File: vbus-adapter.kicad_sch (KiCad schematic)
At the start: 50 parts, among them J1 VBUS, J2 CAN, J3 Sens 2, J4 Sens 1, J5 Power, J6 Backup GPIO, J7 Program, Q1 SS8050, Q2 SS8050, T800 AO3400A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

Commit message: Fix footprint for C802
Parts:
- C802: footprint Capacitor_SMD:CP_Elec_4x3.9 -> Capacitor_SMD:CP_Elec_8x10
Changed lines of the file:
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@@
 			)
 		)
-		(property "Footprint" "Capacitor_SMD:CP_Elec_4x3.9"
+		(property "Footprint" "Capacitor_SMD:CP_Elec_8x10"
 			(at 157.1752 43.18 0)
 			(effects
@@
 			(at 156.21 39.37 0)
 			(effects
+				(font
+					(size 1.27 1.27)
+				)
+				(hide yes)
+			)
+		)
+		(property "Untitled Field" ""
+			(at 156.21 39.37 0)
+			(effects

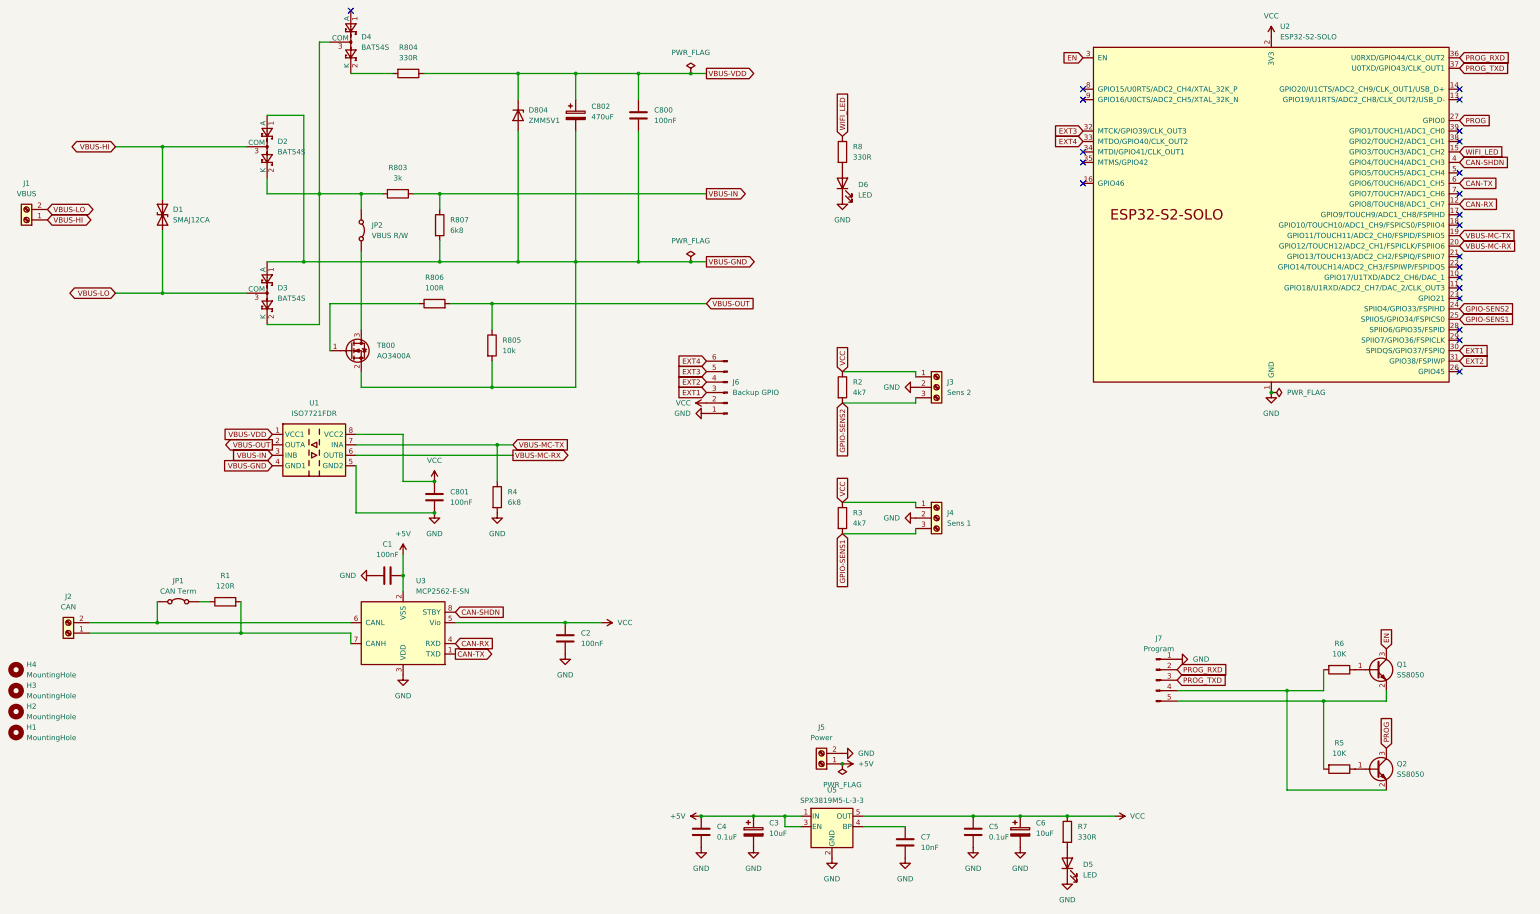
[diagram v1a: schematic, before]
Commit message: Fixed power connection for U3 (MCP2562) Changed Z-Diode to BZY55B5V1RBG with 0805 pinout Added 10k pullup to ESP32 EN pin Added 1uF capacitor to ESP32 EN pin Added 100nF and 10uF capacitor to ESP32 Vcc pin Replaced 0.1uF capacitor values to 100nF for consistency
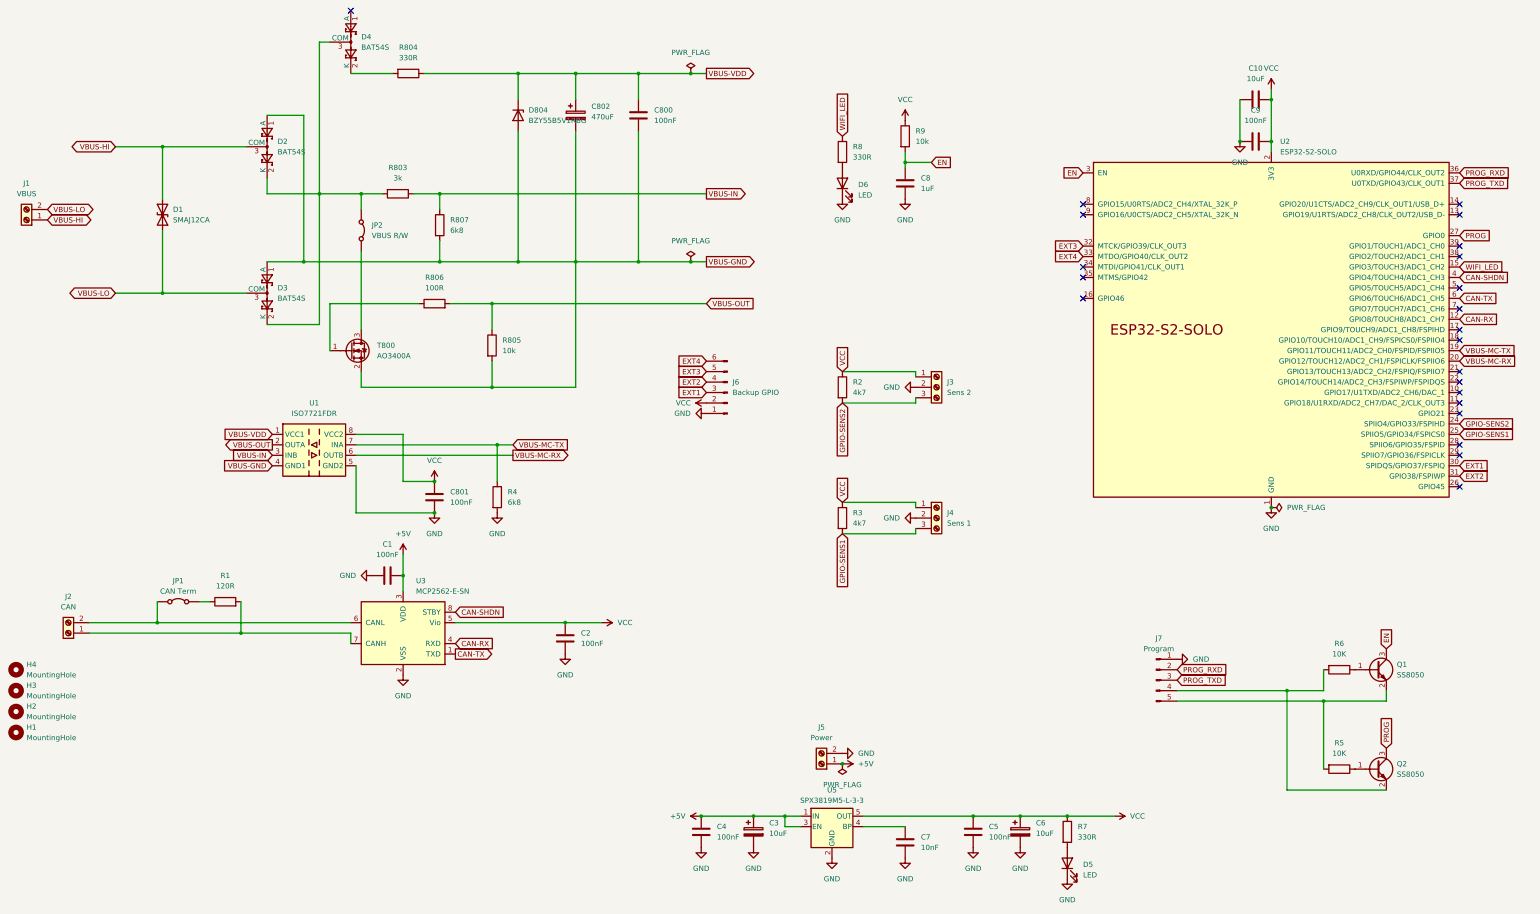
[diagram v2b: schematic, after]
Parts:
- added C10: 10uF, Capacitor_SMD:C_0805_2012Metric, symbol Device:C
- added C8: 1uF, Capacitor_SMD:C_0805_2012Metric, symbol Device:C
- added C9: 100nF, Capacitor_SMD:C_0805_2012Metric, symbol Device:C
- added R9: 10k, Resistor_SMD:R_0805_2012Metric, symbol Device:R
- C4, C5: value 0.1uF -> 100nF
- D804: value ZMM5V1 -> BZY55B5V1RBG; footprint Diode_SMD:D_MiniMELF -> Diode_SMD:D_0805_2012Metric
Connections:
- net +5V: now also U3.3 (VDD); no longer U3.2 (VSS)
- net EN: now also C8.1, R9.2
- net GND: now also U3.2 (VSS), C10.1, C8.2, C9.1; no longer U3.3 (VDD)
- net VCC: now also C10.2, C9.2, R9.1
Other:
- moved on the sheet: U2

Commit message: Version 4
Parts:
- J6: footprint Connector_PinHeader_2.54mm:PinHeader_1x06_P2.54mm_Vertical -> Connector_PinHeader_2.54mm:PinHeader_1x07_P2.54mm_Vertical; symbol Connector:Conn_01x06_Pin -> Connector:Conn_01x07_Pin
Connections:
- net +5V: now also J6.3 (Pin_3)
- net EXT1: now also J6.4 (Pin_4); no longer J6.3 (Pin_3)
- net EXT2: now also J6.5 (Pin_5); no longer J6.4 (Pin_4)
- net EXT3: now also J6.6 (Pin_6); no longer J6.5 (Pin_5)
- net EXT4: now also J6.7 (Pin_7); no longer J6.6 (Pin_6)
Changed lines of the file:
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@@
 	(title_block
 		(title "vbus-adapter")
-		(date "2026-03-06")
-		(rev "v3")
+		(date "2026-04-29")
+		(rev "v4")
 	)
 	(junction
@@
 	)
 	(symbol
+		(lib_id "power:PWR_FLAG")
+		(at 325.12 35.56 270)
+		(unit 1)
+		(exclude_from_sim no)
+		(in_bom yes)
+		(on_board yes)
+		(dnp no)
+		(fields_autoplaced yes)
+		(property "Reference" "#FLG05"
+			(at 327.025 35.56 0)
+			(effects
+				(font
+					(size 1.27 1.27)
+				)
+				(hide yes)
+			)
+		)
+		(property "Value" "PWR_FLAG"
+			(at 328.93 35.5599 90)
+			(effects
+				(font
+					(size 1.27 1.27)
+				)
+				(justify left)
+			)
+		)
+		(property "Footprint" ""
+			(at 325.12 35.56 0)
+			(effects
+				(font
+					(size 1.27 1.27)
+				)
+				(hide yes)
+			)
+		)
+		(property "Datasheet" "~"
+			(at 325.12 35.56 0)
+			(effects
+				(font
+					(size 1.27 1.27)
+				)
+				(hide yes)
+			)
+		)
+		(property "Description" "Special symbol for telling ERC where power comes from"
+			(at 325.12 35.56 0)
+			(effects
+				(font
+					(size 1.27 1.27)
+				)
+				(hide yes)
+			)
+		)
+		(pin "1"
+		)
+		(instances
+			(project ""
+				(path "/c5b76d16-c954-491e-a7b2-87b879d4d4be"
+					(reference "#FLG05")
+					(unit 1)
+				)
+			)
+		)
+	)
+	(symbol
 		(lib_id "Device:C")
 		(at 321.31 45.72 90)
@@
 	(symbol
 		(lib_id "power:GND")
-		(at 187.96 111.76 270)
+		(at 187.96 114.3 270)
 		(unit 1)
 		(exclude_from_sim no)
@@
 		(fields_autoplaced yes)
 		(property "Reference" "#PWR013"
-			(at 181.61 111.76 0)
+			(at 181.61 114.3 0)
 			(effects
 				(font
@@
 		)
 		(property "Value" "GND"
-			(at 184.15 111.7599 90)
+			(at 184.15 114.2999 90)
 			(effects
 				(font
@@
 		)
 		(property "Footprint" ""
-			(at 187.96 111.76 0)
+			(at 187.96 114.3 0)
 			(effects
 				(font
@@
 		)
 		(property "Datasheet" ""
-			(at 187.96 111.76 0)
+			(at 187.96 114.3 0)
 			(effects
 				(font
@@
 		)
 		(property "Description" "Power symbol creates a global label with name \"GND\" , ground"
-			(at 187.96 111.76 0)
+			(at 187.96 114.3 0)
 			(effects
 				(font
@@
 	)
 	(symbol
+		(lib_id "power:+5V")
+		(at 187.96 109.22 90)
+		(unit 1)
+		(exclude_from_sim no)
+		(in_bom yes)
+		(on_board yes)
+		(dnp no)
+		(fields_autoplaced yes)
+		(property "Reference" "#PWR031"
+			(at 191.77 109.22 0)
+			(effects
+				(font
+					(size 1.27 1.27)
+				)
+				(hide yes)
+			)
+		)
+		(property "Value" "+5V"
+			(at 184.15 109.2199 90)
+			(effects
+				(font
+					(size 1.27 1.27)
+				)
+				(justify left)
+			)
+		)
+		(property "Footprint" ""
+			(at 187.96 109.22 0)
+			(effects
+				(font
+					(size 1.27 1.27)
+				)
+				(hide yes)
+			)
+		)
+		(property "Datasheet" ""
+			(at 187.96 109.22 0)
+			(effects
+				(font
+					(size 1.27 1.27)
+				)
+				(hide yes)
+			)
+		)
+		(property "Description" "Power symbol creates a global label with name \"+5V\""
+			(at 187.96 109.22 0)
+			(effects
+				(font
+					(size 1.27 1.27)
+				)
+				(hide yes)
+			)
+		)
+		(pin "1"
+		)
+		(instances
+			(project "vbus-adapter"
+				(path "/c5b76d16-c954-491e-a7b2-87b879d4d4be"
+					(reference "#PWR031")
+					(unit 1)
+				)
+			)
+		)
+	)
+	(symbol
 		(lib_id "power:PWR_FLAG")
 		(at 184.15 29.21 0)
@@
 	(symbol
 		(lib_id "power:VCC")
-		(at 187.96 109.22 90)
+		(at 187.96 111.76 90)
 		(unit 1)
 		(exclude_from_sim no)
@@
 		(fields_autoplaced yes)
 		(property "Reference" "#PWR014"
-			(at 191.77 109.22 0)
+			(at 191.77 111.76 0)
 			(effects
 				(font
@@
 		)
 		(property "Value" "VCC"
-			(at 184.15 109.2199 90)
+			(at 184.15 111.7599 90)
 			(effects
 				(font
@@
 		)
 		(property "Footprint" ""
-			(at 187.96 109.22 0)
+			(at 187.96 111.76 0)
 			(effects
 				(font
@@
 		)
 		(property "Datasheet" ""
-			(at 187.96 109.22 0)
+			(at 187.96 111.76 0)
 			(effects
 				(font
@@
 		)
 		(property "Description" "Power symbol creates a global label with name \"VCC\""
-			(at 187.96 109.22 0)
+			(at 187.96 111.76 0)
 			(effects
 				(font
@@
 	)
 	(symbol
-		(lib_id "Connector:Conn_01x06_Pin")
+		(lib_id "Connector:Conn_01x07_Pin")
 		(at 193.04 106.68 180)
 		(unit 1)
@@
 		(fields_autoplaced yes)
 		(property "Reference" "J6"
-			(at 194.31 104.1399 0)
+			(at 194.31 105.4099 0)
 			(effects
 				(font
@@
 		)
 		(property "Value" "Backup GPIO"
-			(at 194.31 106.6799 0)
+			(at 194.31 107.9499 0)
 			(effects
 				(font
@@
 			)
 		)
-		(property "Footprint" "Connector_PinHeader_2.54mm:PinHeader_1x06_P2.54mm_Vertical"
+		(property "Footprint" "Connector_PinHeader_2.54mm:PinHeader_1x07_P2.54mm_Vertical"
 			(at 193.04 106.68 0)
 			(effects
@@
 			)
 		)
-		(property "Description" "Generic connector, single row, 01x06, script generated"
+		(property "Description" "Generic connector, single row, 01x07, script generated"
+			(at 193.04 106.68 0)
+			(effects
+				(font
+					(size 1.27 1.27)
+				)
+				(hide yes)
+			)
+		)
+		(property "Untitled Field" ""
 			(at 193.04 106.68 0)
 			(effects
@@
 		(pin "5"
 		)
+		(pin "7"
+		)
 		(instances
